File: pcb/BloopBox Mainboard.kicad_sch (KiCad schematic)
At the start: 51 parts, among them J1 ExtLED, J2 SPKR, J3 Raspberry_Pi, J4 I2C, J5 NFC-Module, J6 GPIO, J7 TailBoard, J8 PROG, Q1 2N7002, Q2 2N7002, Q3 2N7002, Q4 2N7002, Q5 2N7002, Q6 2N7002, U1 MAX98357, U2 CAT24C32

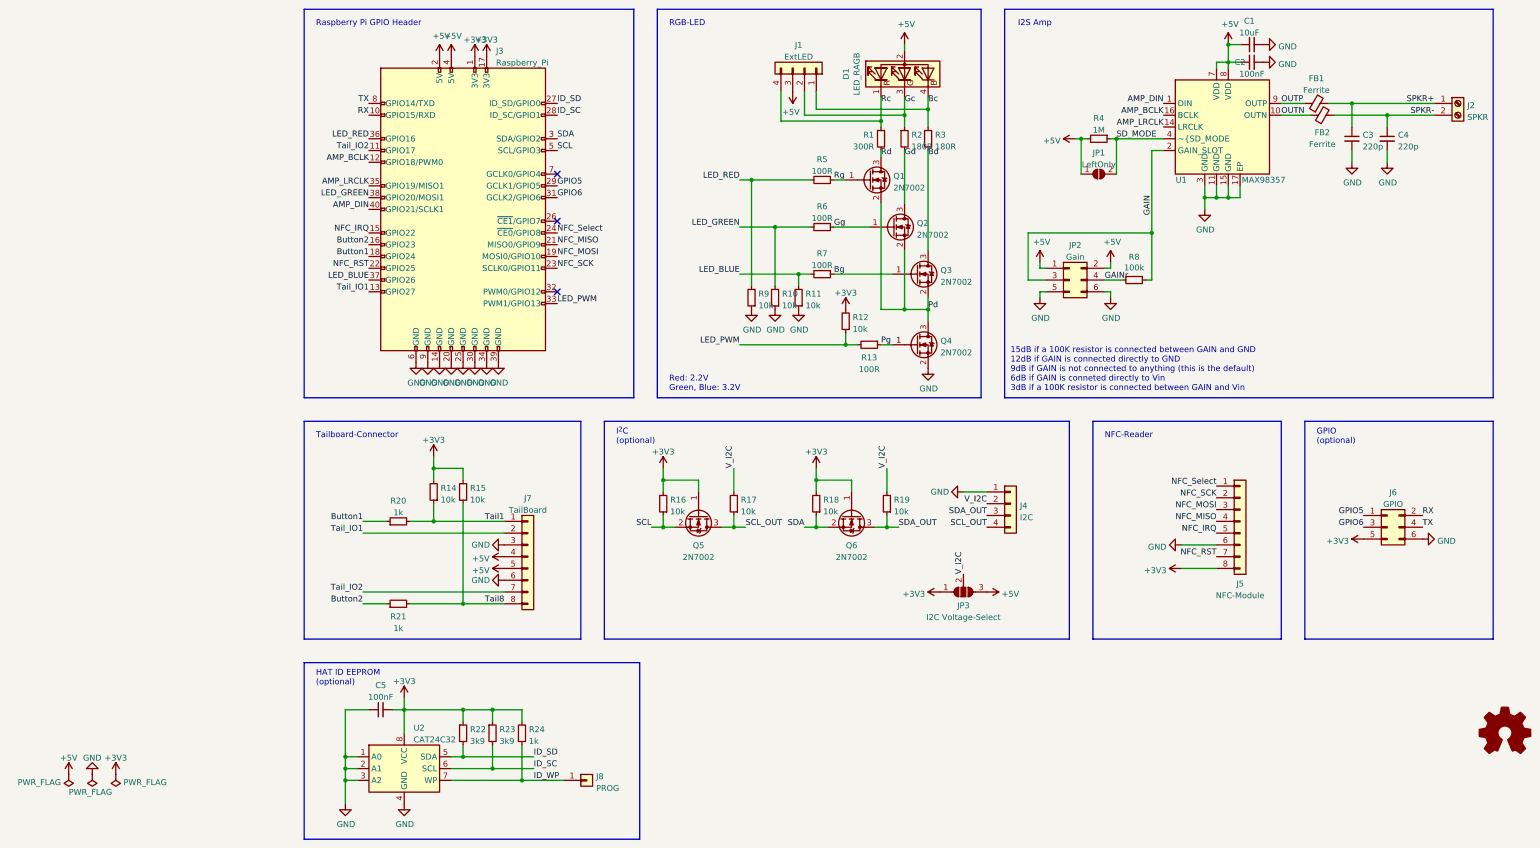
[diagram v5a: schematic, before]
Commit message: feat: remove PWM mosfet
didnt work as hoped so it gets removed
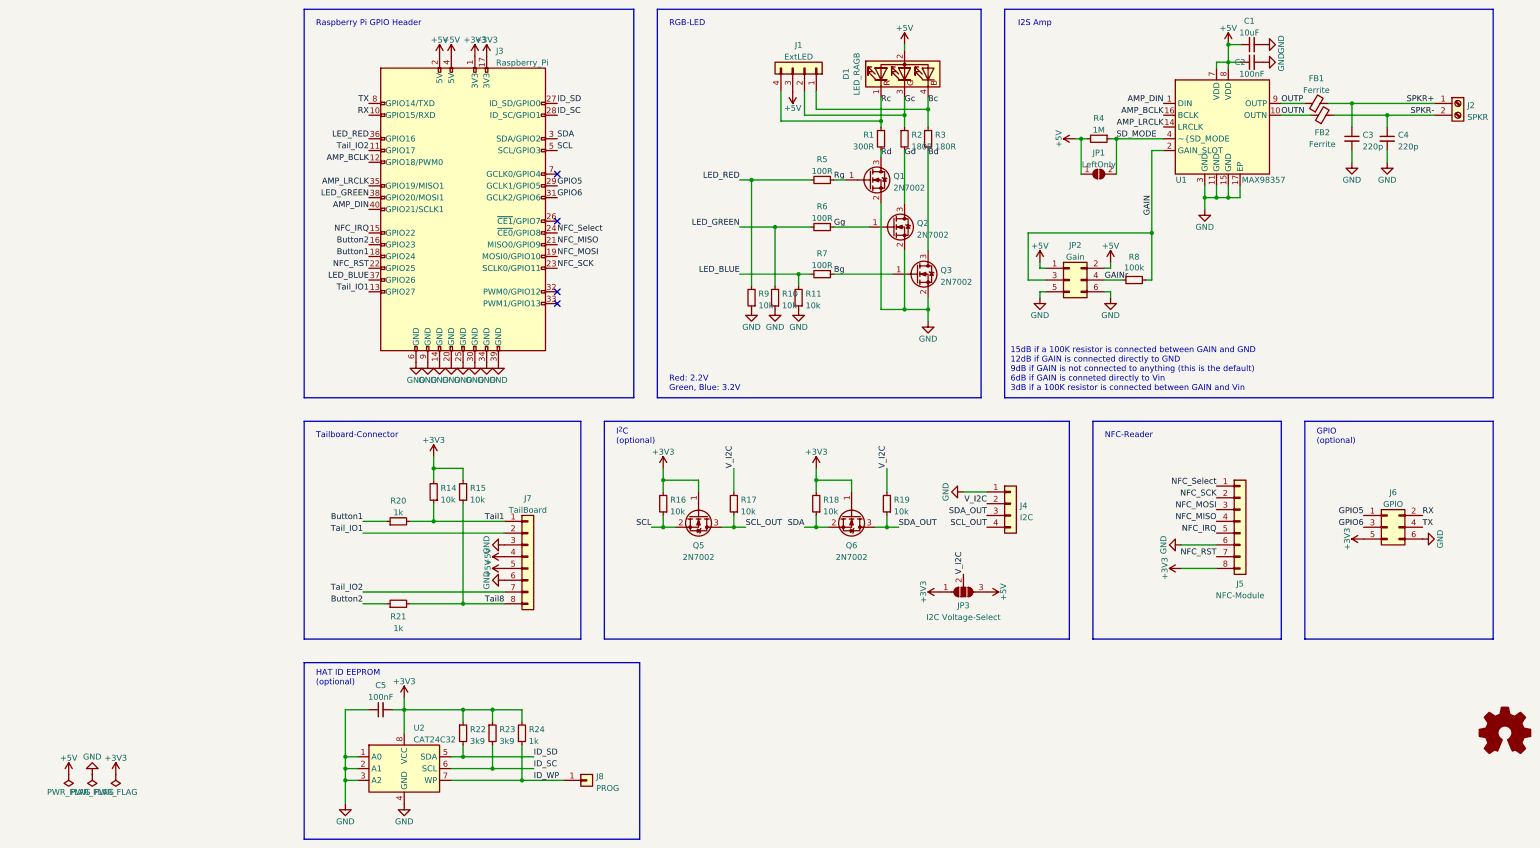
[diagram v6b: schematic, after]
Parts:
- removed Q4: 2N7002, Package_TO_SOT_SMD:SOT-23, symbol Transistor_FET:2N7002
- removed R12: 10k, Resistor_SMD:R_0402_1005Metric, symbol Device:R_Small
- removed R13: 100R, Resistor_SMD:R_0402_1005Metric, symbol Device:R_Small
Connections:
- net Pd is gone; now on net GND: Q1.2 (S), Q2.2 (S), Q3.2 (S)
- net LED_PWM: no longer names the net of J3.33 (PWM1/GPIO13)
- no-connect marks 3 -> 4

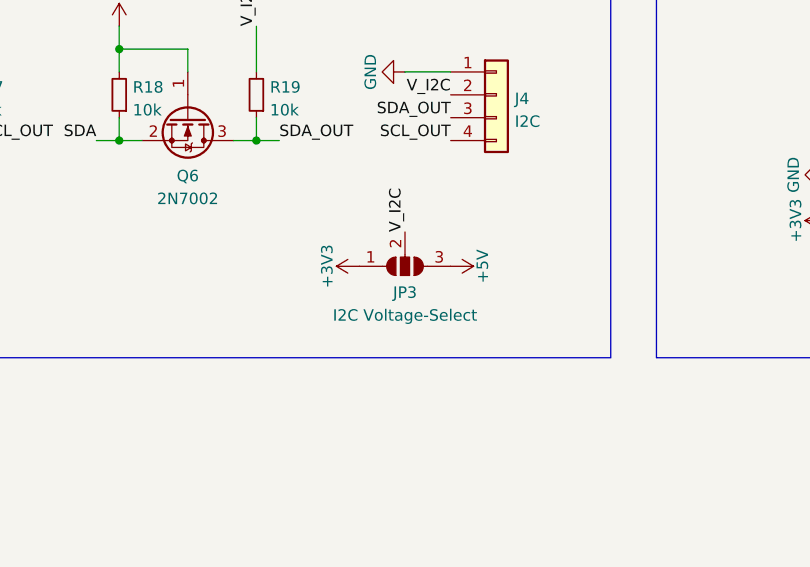
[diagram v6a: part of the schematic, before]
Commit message: fix: add default connection for I2C voltage jumper
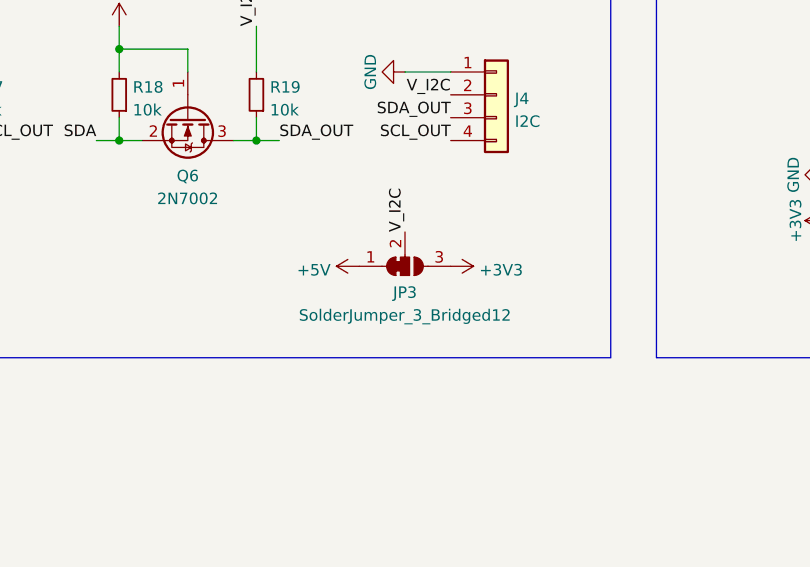
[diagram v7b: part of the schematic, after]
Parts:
- JP3: value I2C Voltage-Select -> SolderJumper_3_Bridged12; footprint Jumper:SolderJumper-3_P1.3mm_Open_RoundedPad1.0x1.5mm -> Jumper:SolderJumper-3_P1.3mm_Bridged12_RoundedPad1.0x1.5mm; symbol Jumper:SolderJumper_3_Open -> Jumper:SolderJumper_3_Bridged12
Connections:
- net +3V3: now also JP3.3 (B); no longer JP3.1 (A)
- net +5V: now also JP3.1 (A); no longer JP3.3 (B)
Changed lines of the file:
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@@
     (pin "2")
   )
-  (symbol (lib_id "Jumper:SolderJumper_3_Open") (at 161.29 143.51 0) (mirror x) (unit 1)
+  (symbol (lib_id "Jumper:SolderJumper_3_Bridged12") (at 161.29 143.51 0) (mirror x) (unit 1)
     (in_bom yes) (on_board yes) (fields_autoplaced)
     (property "Reference" "JP3" (id 0) (at 161.29 146.4294 0))
-    (property "Value" "I2C Voltage-Select" (id 1) (at 161.29 148.9663 0))
-    (property "Footprint" "Jumper:SolderJumper-3_P1.3mm_Open_RoundedPad1.0x1.5mm" (id 2) (at 161.29 143.51 0)
+    (property "Value" "SolderJumper_3_Bridged12" (id 1) (at 161.29 148.9663 0))
+    (property "Footprint" "Jumper:SolderJumper-3_P1.3mm_Bridged12_RoundedPad1.0x1.5mm" (id 2) (at 161.29 143.51 0)
       (effects (font (size 1.27 1.27)) hide)
     )
@@
     (pin "1")
   )
-  (symbol (lib_id "power:+3V3") (at 156.21 143.51 90) (unit 1)
-    (in_bom yes) (on_board yes) (fields_autoplaced)
-    (property "Reference" "#PWR0103" (id 0) (at 160.02 143.51 0)
-      (effects (font (size 1.27 1.27)) hide)
-    )
-    (property "Value" "+3V3" (id 1) (at 152.654 143.51 0))
-    (property "Footprint" "" (id 2) (at 156.21 143.51 0)
-      (effects (font (size 1.27 1.27)) hide)
-    )
-    (property "Datasheet" "" (id 3) (at 156.21 143.51 0)
+  (symbol (lib_id "power:+3V3") (at 166.37 143.51 270) (unit 1)
+    (in_bom yes) (on_board yes) (fields_autoplaced)
+    (property "Reference" "#PWR0103" (id 0) (at 162.56 143.51 0)
+      (effects (font (size 1.27 1.27)) hide)
+    )
+    (property "Value" "+3V3" (id 1) (at 169.545 143.9438 90)
+      (effects (font (size 1.27 1.27)) (justify left))
+    )
+    (property "Footprint" "" (id 2) (at 166.37 143.51 0)
+      (effects (font (size 1.27 1.27)) hide)
+    )
+    (property "Datasheet" "" (id 3) (at 166.37 143.51 0)
       (effects (font (size 1.27 1.27)) hide)
     )
@@
     (pin "1")
   )
-  (symbol (lib_id "power:+5V") (at 166.37 143.51 270) (unit 1)
-    (in_bom yes) (on_board yes) (fields_autoplaced)
-    (property "Reference" "#PWR0114" (id 0) (at 162.56 143.51 0)
-      (effects (font (size 1.27 1.27)) hide)
-    )
-    (property "Value" "+5V" (id 1) (at 169.926 143.51 0))
-    (property "Footprint" "" (id 2) (at 166.37 143.51 0)
-      (effects (font (size 1.27 1.27)) hide)
-    )
-    (property "Datasheet" "" (id 3) (at 166.37 143.51 0)
+  (symbol (lib_id "power:+5V") (at 156.21 143.51 90) (unit 1)
+    (in_bom yes) (on_board yes) (fields_autoplaced)
+    (property "Reference" "#PWR0114" (id 0) (at 160.02 143.51 0)
+      (effects (font (size 1.27 1.27)) hide)
+    )
+    (property "Value" "+5V" (id 1) (at 153.0351 143.9438 90)
+      (effects (font (size 1.27 1.27)) (justify left))
+    )
+    (property "Footprint" "" (id 2) (at 156.21 143.51 0)
+      (effects (font (size 1.27 1.27)) hide)
+    )
+    (property "Datasheet" "" (id 3) (at 156.21 143.51 0)
       (effects (font (size 1.27 1.27)) hide)
     )
@@
     )
     (path "/0c340d81-1114-48d4-8b01-dcb498ebcbcf"
-      (reference "JP3") (unit 1) (value "I2C Voltage-Select") (footprint "Jumper:SolderJumper-3_P1.3mm_Open_RoundedPad1.0x1.5mm")
+      (reference "JP3") (unit 1) (value "SolderJumper_3_Bridged12") (footprint "Jumper:SolderJumper-3_P1.3mm_Bridged12_RoundedPad1.0x1.5mm")
     )
     (path "/127958e6-6cc6-42dc-9293-0f5a54cf0273"

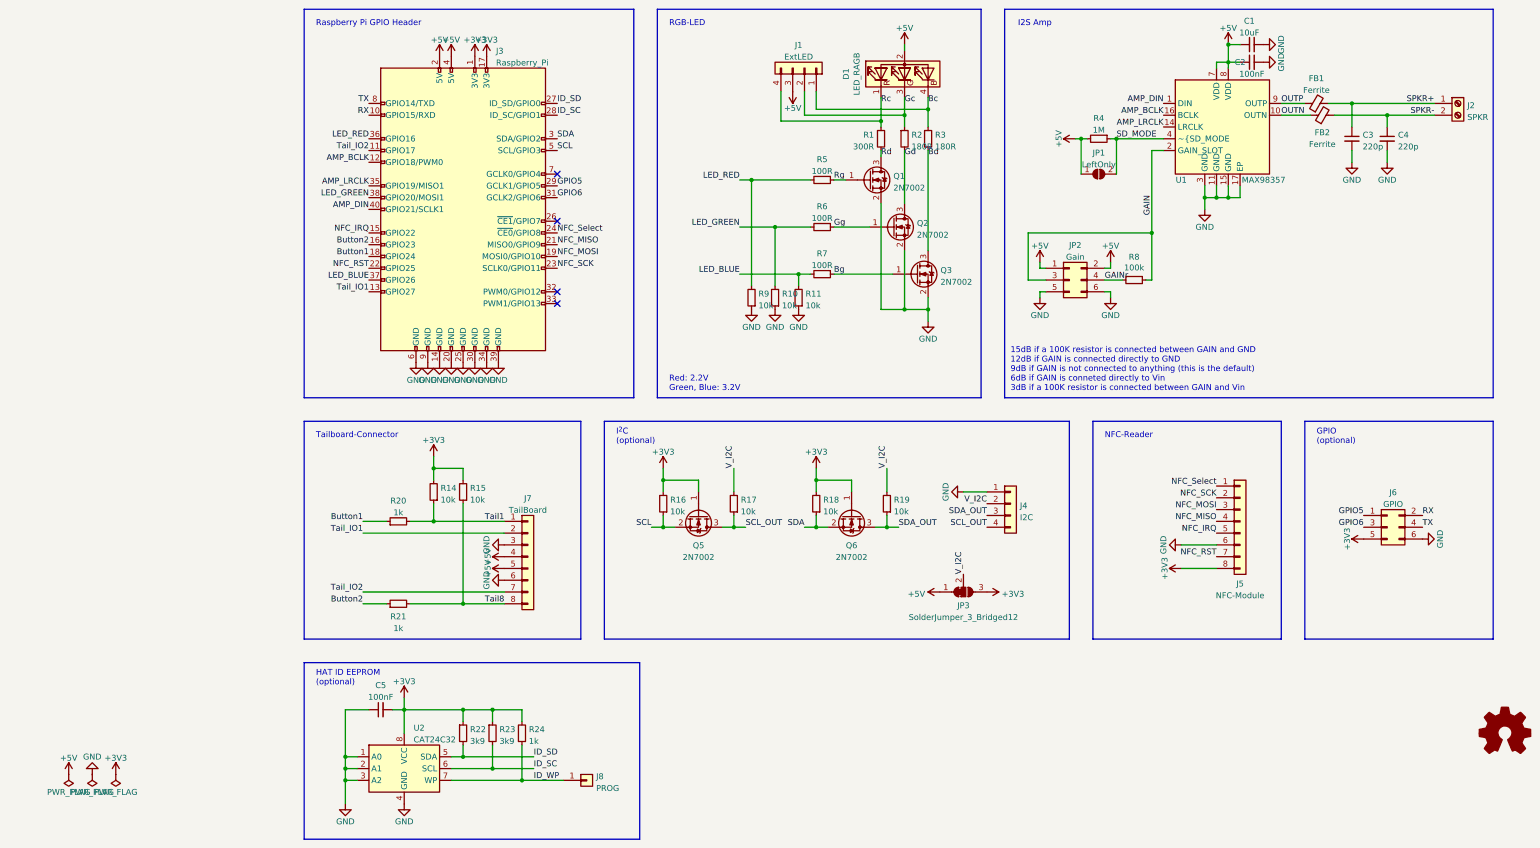
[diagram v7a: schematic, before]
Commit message: feat!: remove RGB LED
remove the RGB LED facilities since we're using I2C for that now
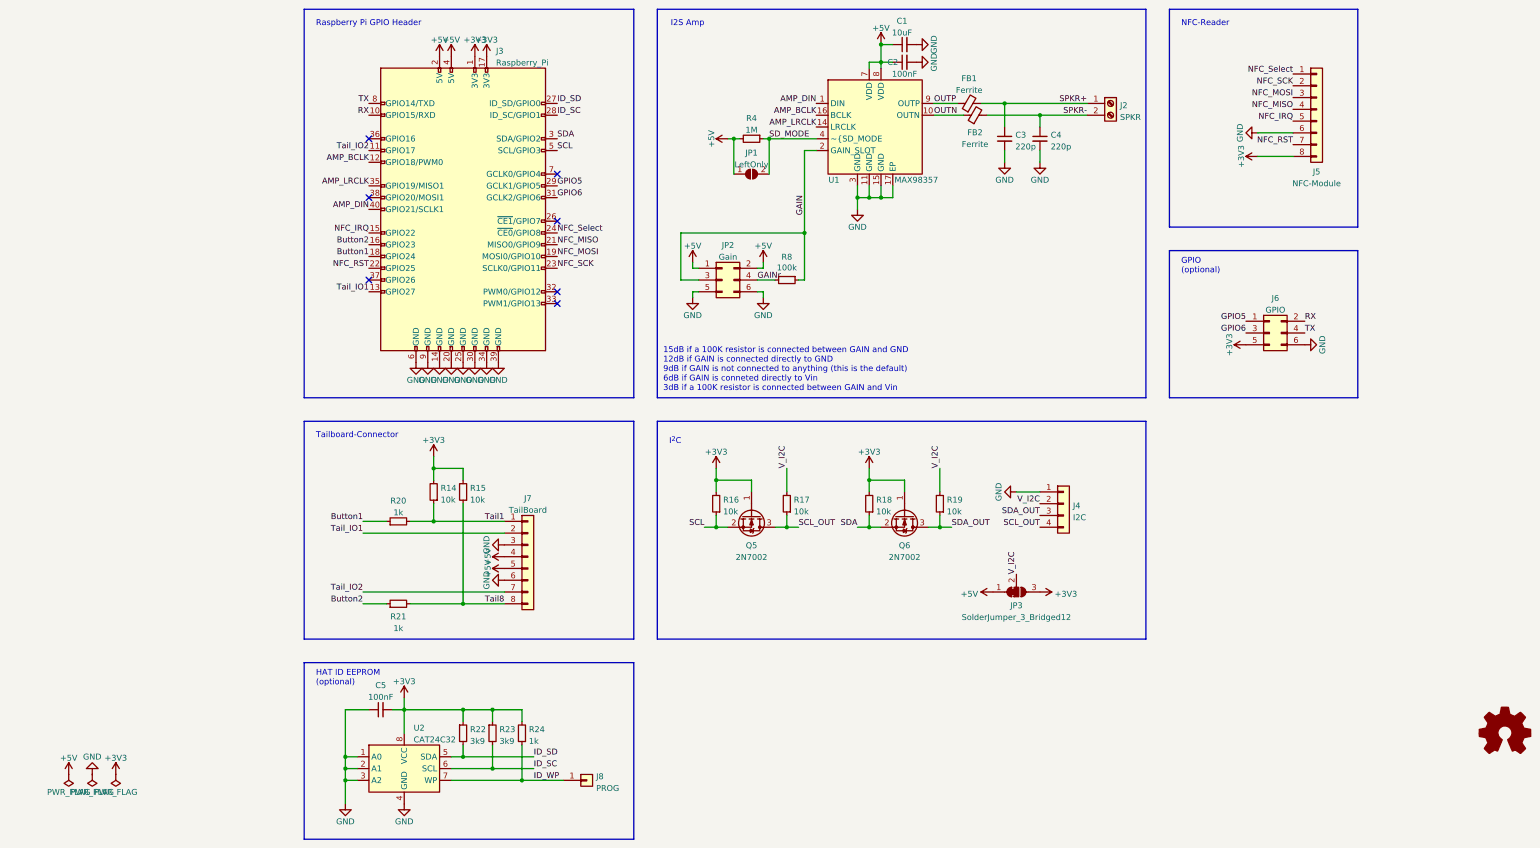
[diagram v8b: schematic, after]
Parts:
- removed D1: LED_RAGB, LED_THT:LED_D5.0mm-4_RGB_Staggered_Pins, symbol Device:LED_RAGB
- removed J1: ExtLED, Connector_JST:JST_PH_S4B-PH-K_1x04_P2.00mm_Horizontal, symbol Connector_Generic:Conn_01x04
- removed Q1, Q2, Q3: 2N7002, Package_TO_SOT_SMD:SOT-23, symbol Transistor_FET:2N7002
- removed R1: 300R, Resistor_SMD:R_0603_1608Metric, symbol Device:R_Small
- removed R10, R11, R9: 10k, Resistor_SMD:R_0402_1005Metric, symbol Device:R_Small
- removed R2, R3: 180R, Resistor_SMD:R_0603_1608Metric, symbol Device:R_Small
- removed R5, R6, R7: 100R, Resistor_SMD:R_0402_1005Metric, symbol Device:R_Small
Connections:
- net LED_BLUE: no longer names the net of J3.37 (GPIO26)
- net LED_GREEN: no longer names the net of J3.38 (GPIO20/MOSI1)
- net LED_RED: no longer names the net of J3.36 (GPIO16)
- no-connect marks 4 -> 7
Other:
- note added: "I^{2}C"
- note removed: "I^{2}C (optional)"
- note removed: "RGB-LED"
- note removed: "Red: 2.2V Green, Blue: 3.2V"
- moved on the sheet: C1, C2, C3, C4, FB1, FB2, J2, J4, J5, J6, JP1, JP2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
